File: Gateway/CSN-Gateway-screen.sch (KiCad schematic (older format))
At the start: 17 parts, among them IC2 FT232RL, P1 USB_MINI, P2 CONN_01X12, P4 CONN_OLED_SCREEN, SW1 SW_PUSH, SW2 SW_PUSH

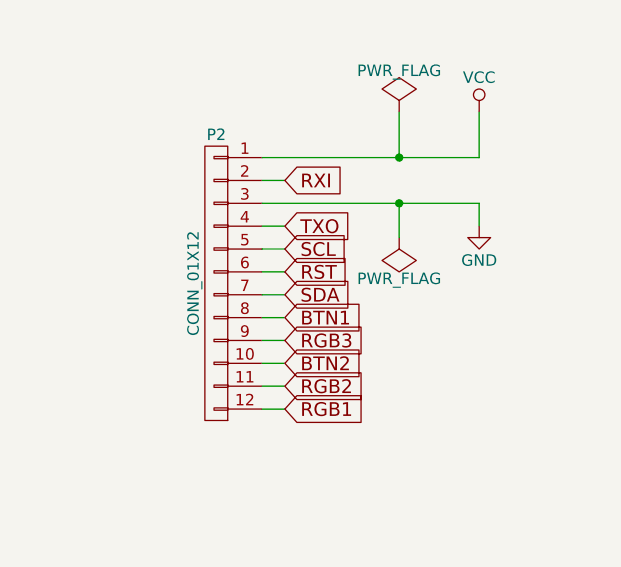
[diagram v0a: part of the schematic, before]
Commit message: add all missing footprints
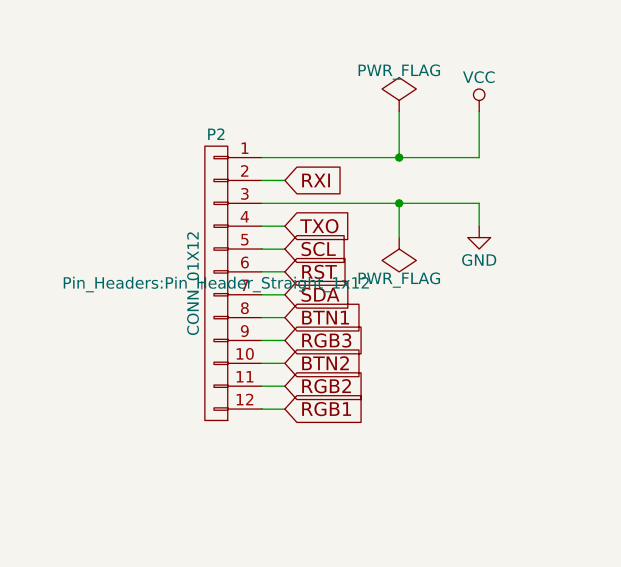
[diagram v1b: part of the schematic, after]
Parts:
- D1: footprint (none) -> footprints:LedRGB_MULTICOMP_703-1028
- P1: footprint (none) -> footprints:MolexUSB_Mini-B_67503-1020
- P2: footprint (none) -> Pin_Headers:Pin_Header_Straight_1x12
- P4: footprint (none) -> Socket_Strips:Socket_Strip_Straight_1x04
- SW1, SW2: footprint (none) -> Buttons_Switches_ThroughHole:SW_PUSH_6mm
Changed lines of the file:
@@
 LIBS:mysensors_sensors
 LIBS:gateway
+LIBS:CSN-Gateway-screen-cache
 EELAYER 25 0
 EELAYER END
@@
 F 0 "P4" H 9250 2750 50  0000 C CNN
 F 1 "CONN_OLED_SCREEN" V 9350 2500 50  0000 C CNN
-F 2 "" H 9250 2500 50  0001 C CNN
+F 2 "Socket_Strips:Socket_Strip_Straight_1x04" H 9250 2500 50  0001 C CNN
 F 3 "" H 9250 2500 50  0000 C CNN
 	1    9250 2500
@@
 F 0 "SW1" H 9300 4560 50  0000 C CNN
 F 1 "SW_PUSH" H 9150 4370 50  0000 C CNN
-F 2 "" H 9150 4450 50  0001 C CNN
+F 2 "Buttons_Switches_ThroughHole:SW_PUSH_6mm" H 9150 4450 50  0001 C CNN
 F 3 "" H 9150 4450 50  0000 C CNN
 	1    9150 4450
@@
 F 0 "D1" H 6225 4600 50  0000 C CNN
 F 1 "LED_RABG" H 6175 3900 50  0000 C CNN
-F 2 "" H 6100 4200 50  0001 C CNN
+F 2 "footprints:LedRGB_MULTICOMP_703-1028" H 6100 4200 50  0001 C CNN
 F 3 "" H 6100 4200 50  0000 C CNN
 	1    6150 4250
@@
 F 0 "P1" H 4825 1675 50  0000 C CNN
 F 1 "USB_MINI" H 4500 2000 50  0000 C CNN
-F 2 "" V 4450 1700 50  0001 C CNN
+F 2 "footprints:MolexUSB_Mini-B_67503-1020" V 4450 1700 50  0001 C CNN
 F 3 "" V 4450 1700 50  0000 C CNN
 	1    4500 1800
@@
 F 0 "SW2" H 8400 4560 50  0000 C CNN
 F 1 "SW_PUSH" H 8250 4370 50  0000 C CNN
-F 2 "" H 8250 4450 50  0001 C CNN
+F 2 "Buttons_Switches_ThroughHole:SW_PUSH_6mm" H 8250 4450 50  0001 C CNN
 F 3 "" H 8250 4450 50  0000 C CNN
 	1    8250 4450
@@
 F 0 "P2" H 2550 4350 50  0000 C CNN
 F 1 "CONN_01X12" V 2650 3700 50  0000 C CNN
-F 2 "" H 2550 3700 50  0000 C CNN
+F 2 "Pin_Headers:Pin_Header_Straight_1x12" H 2550 3700 50  0000 C CNN
 F 3 "" H 2550 3700 50  0000 C CNN
 	1    2550 3700

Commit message: finish screen pcb routing
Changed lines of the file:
@@
 F 3 "" H 9250 2500 50  0000 C CNN
 	1    9250 2500
-	1    0    0    -1
+	1    0    0    1
 $EndComp
 $Comp
 L GND #PWR01
 U 1 1 583827DD
-P 8800 2900
-F 0 "#PWR01" H 8800 2650 50  0001 C CNN
-F 1 "GND" H 8800 2750 50  0000 C CNN
-F 2 "" H 8800 2900 50  0000 C CNN
-F 3 "" H 8800 2900 50  0000 C CNN
-	1    8800 2900
+P 8950 2800
+F 0 "#PWR01" H 8950 2550 50  0001 C CNN
+F 1 "GND" H 8950 2650 50  0000 C CNN
+F 2 "" H 8950 2800 50  0000 C CNN
+F 3 "" H 8950 2800 50  0000 C CNN
+	1    8950 2800
 	1    0    0    -1
 $EndComp
@@
 L VCC #PWR02
 U 1 1 58382807
-P 9000 2900
-F 0 "#PWR02" H 9000 2750 50  0001 C CNN
-F 1 "VCC" H 9000 3050 50  0000 C CNN
-F 2 "" H 9000 2900 50  0000 C CNN
-F 3 "" H 9000 2900 50  0000 C CNN
-	1    9000 2900
-	-1   0    0    1
+P 8550 2200
+F 0 "#PWR02" H 8550 2050 50  0001 C CNN
+F 1 "VCC" H 8550 2350 50  0000 C CNN
+F 2 "" H 8550 2200 50  0000 C CNN
+F 3 "" H 8550 2200 50  0000 C CNN
+	1    8550 2200
+	1    0    0    -1
 $EndComp
 Text GLabel 8950 2450 0    60   Input ~ 0
@@
 $EndComp
 Wire Wire Line
-	9050 2650 9000 2650
-Wire Wire Line
-	9000 2650 9000 2900
-Wire Wire Line
-	8800 2900 8800 2550
-Wire Wire Line
-	8800 2550 9050 2550
-Wire Wire Line
-	8950 2350 9050 2350
-Wire Wire Line
-	9050 2450 8950 2450
-Wire Wire Line
 	7100 1300 7250 1300
 Wire Wire Line
@@
 	3700 3350 3700 3450
 Text GLabel 2850 3250 2    60   Input ~ 0
-RXI
+TXO
 Wire Wire Line
 	2750 3250 2850 3250
 Text GLabel 2850 3450 2    60   Input ~ 0
-TXO
+RXI
 Wire Wire Line
 	2750 3450 2850 3450
@@
 	3350 2950 3350 3150
 Connection ~ 3350 3150
+Wire Wire Line
+	9050 2650 8950 2650
+Wire Wire Line
+	8950 2650 8950 2800
+Wire Wire Line
+	8550 2200 8550 2550
+Wire Wire Line
+	8550 2550 9050 2550
+Wire Wire Line
+	8950 2450 9050 2450
+Wire Wire Line
+	9050 2350 8950 2350
 $EndSCHEMATC

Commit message: fix wrong footprints
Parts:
- D1: symbol LED_RABG -> LED_RABG-RESCUE-CSN-Gateway-screen-RESCUE-CSN-Gateway-screen
- P1: symbol USB_OTG -> USB_OTG-RESCUE-CSN-Gateway-screen
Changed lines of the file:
@@
 EESchema Schematic File Version 2
+LIBS:CSN-Gateway-screen-rescue
 LIBS:power
 LIBS:device
@@
 $EndComp
 $Comp
-L LED_RABG D1
+L LED_RABG-RESCUE-CSN-Gateway-screen-RESCUE-CSN-Gateway-screen D1
 U 1 1 5839ED83
 P 6150 4250
@@
 NoConn ~ 7100 2100
 $Comp
-L USB_OTG P1
+L USB_OTG-RESCUE-CSN-Gateway-screen P1
 U 1 1 583B4C2E
 P 4500 1800
@@
 	3700 3350 3700 3450
 Text GLabel 2850 3250 2    60   Input ~ 0
-TXO
+RXI
 Wire Wire Line
 	2750 3250 2850 3250
 Text GLabel 2850 3450 2    60   Input ~ 0
-RXI
+TXO
 Wire Wire Line
 	2750 3450 2850 3450

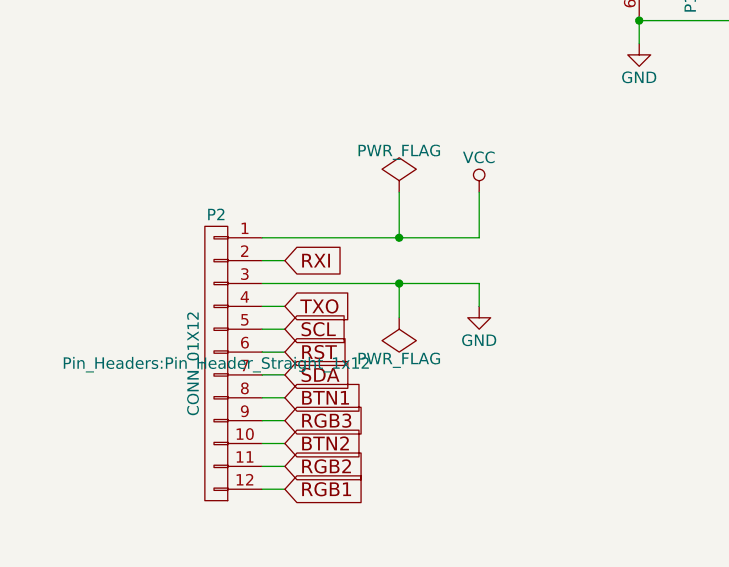
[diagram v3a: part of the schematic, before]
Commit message: Fix footprints for power supply components
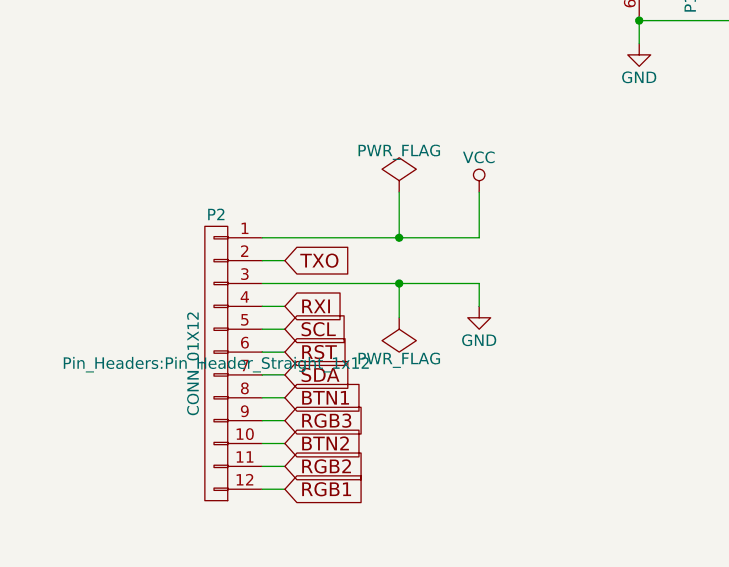
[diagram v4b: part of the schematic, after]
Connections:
- net RXI: now also P2.4 (P4); no longer P2.2 (P2)
- net TXO: now also P2.2 (P2); no longer P2.4 (P4)
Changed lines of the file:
@@
 	3700 3350 3700 3450
 Text GLabel 2850 3250 2    60   Input ~ 0
-RXI
+TXO
 Wire Wire Line
 	2750 3250 2850 3250
 Text GLabel 2850 3450 2    60   Input ~ 0
-TXO
+RXI
 Wire Wire Line
 	2750 3450 2850 3450
